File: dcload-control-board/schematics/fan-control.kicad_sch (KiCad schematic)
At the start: 16 parts, among them J500 Conn_01x04_Male, J501 Conn_01x04_Male

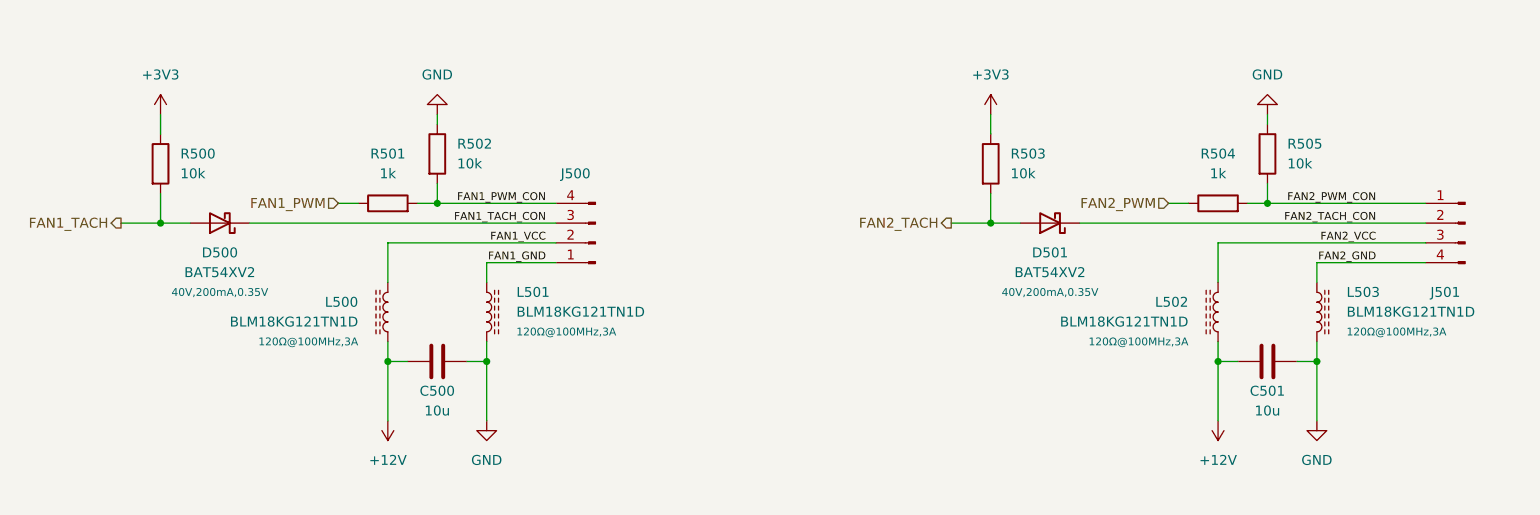
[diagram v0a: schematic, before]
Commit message: add: interface panel board
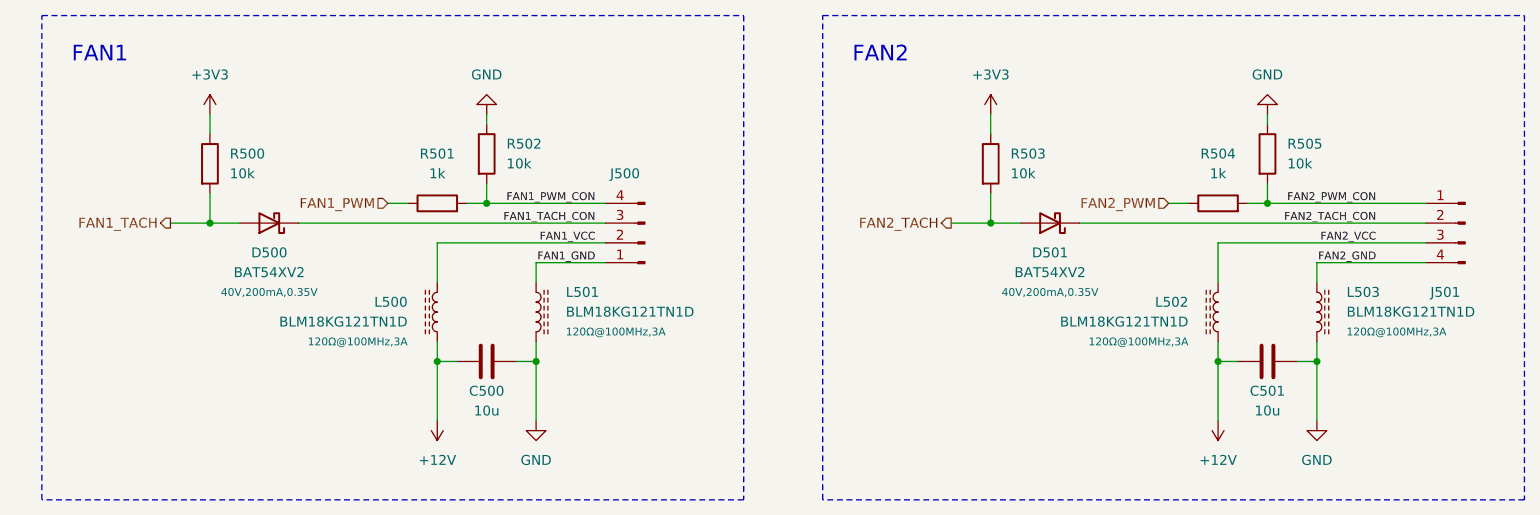
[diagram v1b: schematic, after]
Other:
- note added: "FAN1"
- note added: "FAN2"
- moved on the sheet: C500, D500, J500, L500, L501, R500, R501, R502
